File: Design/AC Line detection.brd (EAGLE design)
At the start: 17 x 20 mm, 14 parts

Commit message: version 1.0
* Added production files
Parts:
- moved FID2 19.4 mm to (4.49, 2.16)
- moved FID1 14.7 mm to (6.80, 19.0)
- moved LOGO1 1.22 mm to (9.08, 7.91)
- moved U$1 0.64 mm to (13.5, 1.25)
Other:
- board text added: "AC-IN"
- board text added: "~"
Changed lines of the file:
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@@
 <layer number="20" name="Dimension" color="15" fill="1" visible="yes" active="yes"/>
 <layer number="21" name="tPlace" color="7" fill="1" visible="yes" active="yes"/>
-<layer number="22" name="bPlace" color="7" fill="1" visible="yes" active="yes"/>
+<layer number="22" name="bPlace" color="7" fill="1" visible="no" active="yes"/>
 <layer number="23" name="tOrigins" color="15" fill="1" visible="yes" active="yes"/>
 <layer number="24" name="bOrigins" color="15" fill="1" visible="yes" active="yes"/>
@@
 <layer number="35" name="tGlue" color="7" fill="4" visible="no" active="yes"/>
 <layer number="36" name="bGlue" color="7" fill="5" visible="no" active="yes"/>
-<layer number="37" name="tTest" color="7" fill="1" visible="yes" active="yes"/>
-<layer number="38" name="bTest" color="7" fill="1" visible="yes" active="yes"/>
+<layer number="37" name="tTest" color="14" fill="1" visible="yes" active="yes"/>
+<layer number="38" name="bTest" color="11" fill="1" visible="yes" active="yes"/>
 <layer number="39" name="tKeepout" color="4" fill="11" visible="no" active="yes"/>
 <layer number="40" name="bKeepout" color="1" fill="11" visible="no" active="yes"/>
@@
 <layer number="118" name="Rect_Pads" color="7" fill="1" visible="no" active="no"/>
 <layer number="119" name="Logo" color="10" fill="1" visible="no" active="yes"/>
-<layer number="121" name="_tsilk" color="7" fill="1" visible="yes" active="yes"/>
-<layer number="122" name="_bsilk" color="7" fill="1" visible="yes" active="yes"/>
+<layer number="121" name="_tsilk" color="14" fill="1" visible="yes" active="yes"/>
+<layer number="122" name="_bsilk" color="11" fill="1" visible="yes" active="yes"/>
 <layer number="123" name="tTestmark" color="7" fill="1" visible="no" active="yes"/>
 <layer number="124" name="bTestmark" color="7" fill="1" visible="no" active="yes"/>
@@
 <wire x1="15" y1="20" x2="2" y2="20" width="0.2" layer="20"/>
 <wire x1="2" y1="20" x2="0" y2="18" width="0.2" layer="20" curve="90"/>
-<text x="11.32035" y="19.71355" size="1.27" layer="20" font="vector" ratio="10" rot="R180">S</text>
-<text x="13.91445" y="19.71355" size="1.27" layer="20" font="vector" ratio="10" rot="R180">+</text>
-<text x="16.39225" y="19.71355" size="1.27" layer="20" font="vector" ratio="10" rot="R180">-</text>
-<text x="2.6342" y="0.18125" size="0.8128" layer="121" font="vector">AC LINE DETECTOR</text>
+<text x="11.32035" y="19.71355" size="1.27" layer="121" font="vector" ratio="15" rot="R180">S</text>
+<text x="13.8428" y="19.71355" size="1.27" layer="121" font="vector" ratio="15" rot="R180">+</text>
+<text x="16.1063" y="19.726" size="1.27" layer="121" font="vector" ratio="15" rot="R180">-</text>
+<text x="2.67895" y="0.19615" size="0.8128" layer="121" font="vector" ratio="10">AC LINE DETECTOR</text>
 <dimension x1="15" y1="20" x2="15" y2="0" x3="24" y3="10" textsize="0.8128" layer="47"/>
 <dimension x1="0" y1="2" x2="17" y2="2" x3="8.5" y3="-6" textsize="0.8128" layer="47"/>
@@
 </polygon>
 <text x="9.77905" y="0.1472" size="1.016" layer="16" font="vector" ratio="15" rot="MR0">V1.0</text>
+<text x="7.93115" y="18.0174" size="1.4224" layer="122" ratio="15" rot="MR0">AC-IN</text>
+<text x="2.73015" y="12.7392" size="1.778" layer="122" font="vector" ratio="15">~</text>
+<text x="6.22115" y="12.72425" size="1.778" layer="122" font="vector" ratio="15">~</text>
 </plain>
 <attributes>
@@
 <elements>
 <element name="B1" library="rectifier" library_urn="urn:adsk.eagle:library:336" package="DBS" value="DBS107G" x="4.39805" y="6.71345"/>
-<element name="FID1" library="edwinRobotics" package="FIDUCIAL_1MM" value="FIDUCIAL&quot;&quot;" x="1.19485" y="5.33225"/>
-<element name="FID2" library="edwinRobotics" package="FIDUCIAL_1MM" value="FIDUCIAL&quot;&quot;" x="14.5243" y="18.77995"/>
-<element name="LOGO1" library="edwinRobotics" package="OSHW-LOGO-MINI" value="OSHW-LOGOMINI" x="7.86095" y="7.95625" rot="MR0"/>
-<element name="U$1" library="edwinRobotics" package="LOGO-9.5MMX4.5MM" value="LOGO-9.5MMX4.5MM" x="12.88175" y="1.2996" rot="MR0"/>
+<element name="FID1" library="edwinRobotics" package="FIDUCIAL_1MM" value="FIDUCIAL&quot;&quot;" x="6.802" y="18.9554"/>
+<element name="FID2" library="edwinRobotics" package="FIDUCIAL_1MM" value="FIDUCIAL&quot;&quot;" x="4.49175" y="2.1645"/>
+<element name="LOGO1" library="edwinRobotics" package="OSHW-LOGO-MINI" value="OSHW-LOGOMINI" x="9.08385" y="7.91165" rot="MR0"/>
+<element name="U$1" library="edwinRobotics" package="LOGO-9.5MMX4.5MM" value="LOGO-9.5MMX4.5MM" x="13.5252" y="1.255" rot="MR0"/>
 <element name="R1" library="edwinRobotics" package="R0603" value="10k" x="11.51635" y="13.9717"/>
 <element name="R2" library="edwinRobotics" package="R0603" value="390k" x="9.80565" y="2.4757" rot="R270"/>

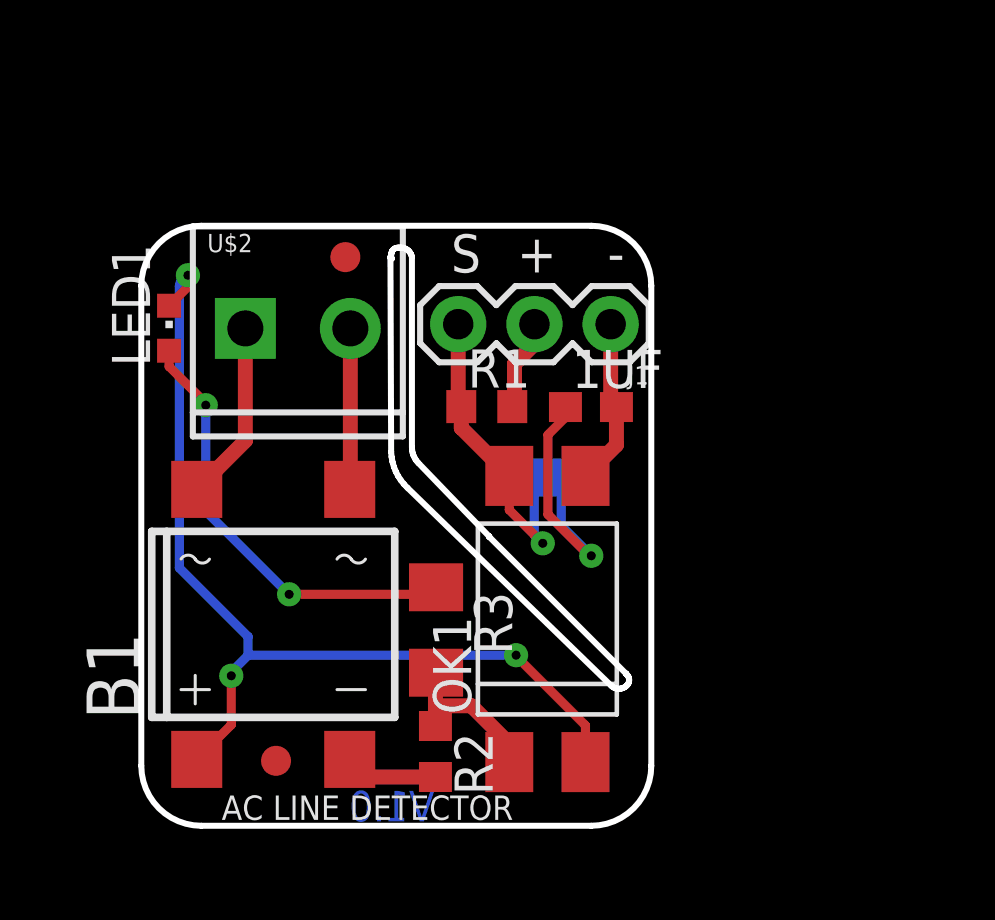
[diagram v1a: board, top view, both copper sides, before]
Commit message: Version 1.0
* updated schematics: Added electrolytic capacitor on board
* Updated board: increased dimesnions and new routing
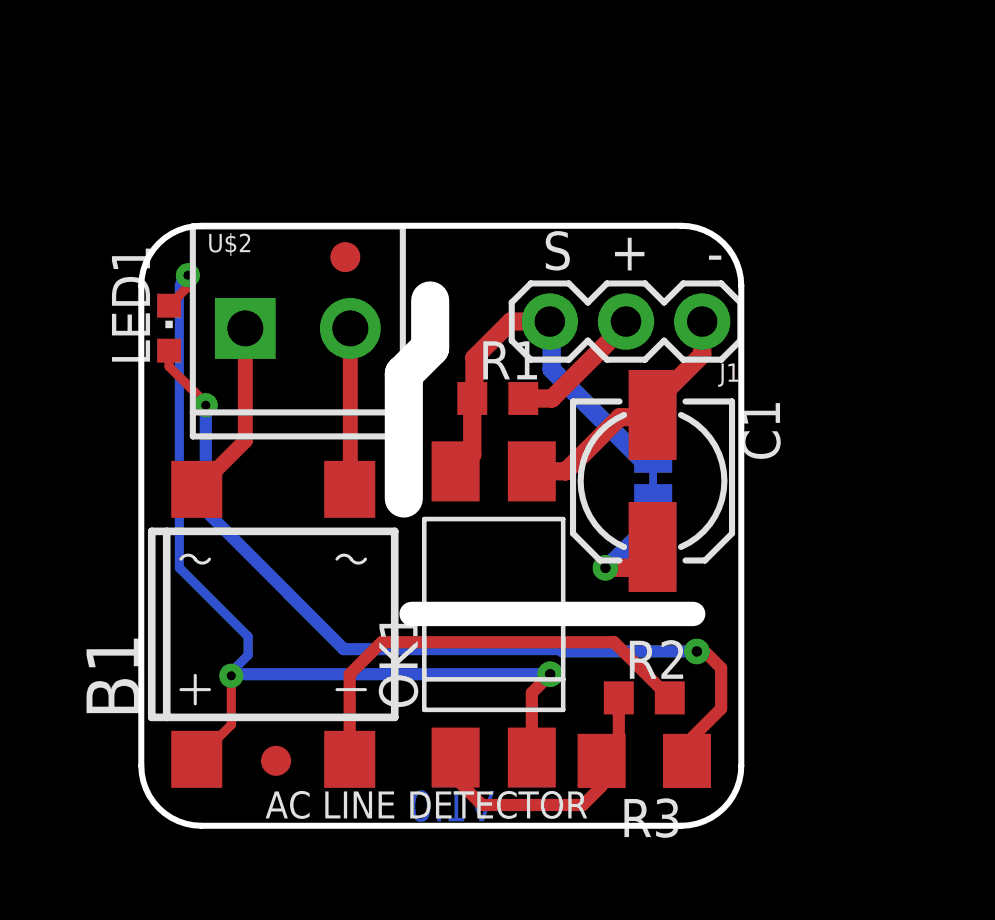
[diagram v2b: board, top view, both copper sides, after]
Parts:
- removed 1UF: (no value), edwinRobotics:C0603
- removed JP2: JUMPER-SMT_2_NO_SILK, edwinRobotics:SMT-JUMPER_2_NO_SILK
- added C1: (no value), edwinRobotics:153CLV-0505
- added JP1: JUMPER-SMT_2_NC_TRACE_NO-SILK, edwinRobotics:SMT-JUMPER_2_NC_TRACE_NO-SILK
- moved R3 8.20 mm to (16.8, 2.16), turned to 180 degrees
- moved R2 7.19 mm to (16.8, 4.26), turned to 0 degrees
- moved J1 3.05 mm to (18.7, 16.8)
- moved OK1 1.79 mm to (11.7, 7.04)
- moved LOGO1 1.15 mm to (9.89, 8.73)
- moved U$1 1.00 mm to (14.5, 1.25)
- moved R1 0.46 mm to (11.9, 14.2)
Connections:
- net GND: now also C1.-; no longer 1UF.2
- net N$2: now also C1.+, JP1.2; no longer 1UF.1, JP2.2
- net SIGNAL: now also JP1.1; no longer JP2.1
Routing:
- net N$3: track 14.8 -> 28.8 mm
- net N$1: track 3.10 -> 14.7 mm
- net +: track 5.38 -> 9.43 mm
- net N$2: track 8.94 -> 5.04 mm
- net GND: track 5.69 -> 8.72 mm
- net SIGNAL: track 10.8 -> 13.4 mm, vias 1 -> 0
- net 5V: track 3.05 -> 4.54 mm
- net -: track 32.8 -> 33.5 mm
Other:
- board size 17 x 20 mm -> 20 x 20 mm

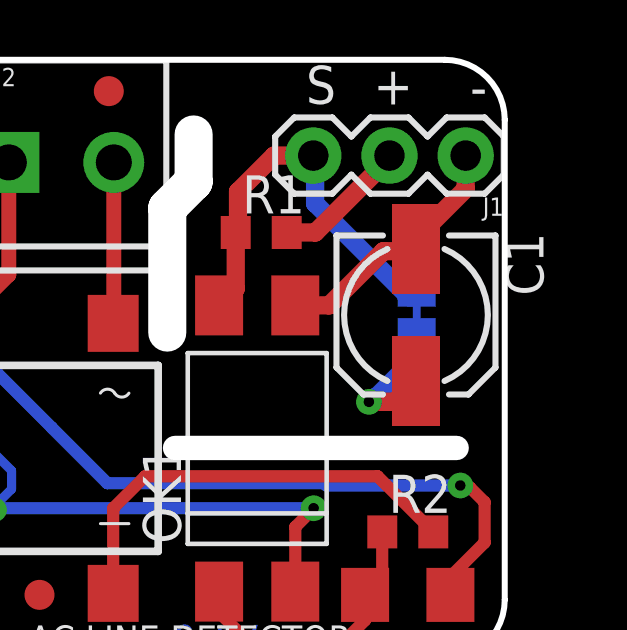
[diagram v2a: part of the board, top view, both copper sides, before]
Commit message: version 1.0 update:
* Updated Capacitor Pad Size
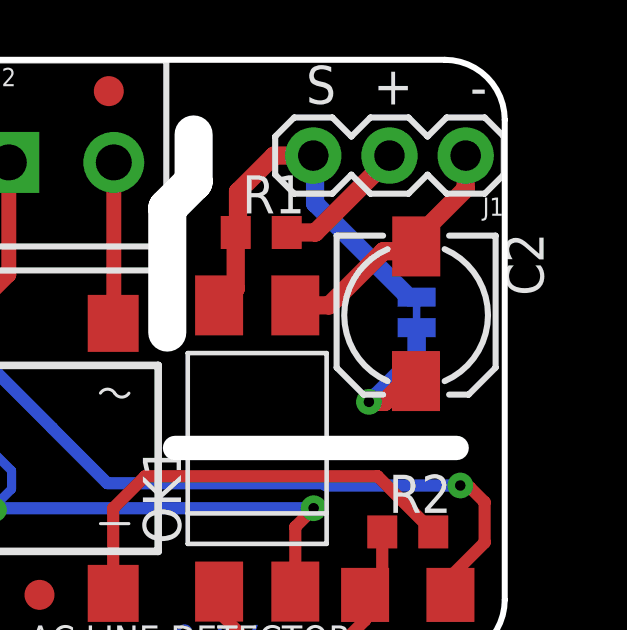
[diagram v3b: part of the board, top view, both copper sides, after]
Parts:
- removed C1: (no value), edwinRobotics:153CLV-0505
- added C2: 2.2uF, edwinRobotics:CAPACITOR-2.2UF_4X5MM_JENNY
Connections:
- net GND: now also C2.-; no longer C1.-
- net N$2: now also C2.+; no longer C1.+
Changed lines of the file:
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@@
 <layer number="19" name="Unrouted" color="6" fill="1" visible="yes" active="yes"/>
 <layer number="20" name="Dimension" color="15" fill="1" visible="yes" active="yes"/>
-<layer number="21" name="tPlace" color="7" fill="1" visible="yes" active="yes"/>
+<layer number="21" name="tPlace" color="7" fill="1" visible="no" active="yes"/>
 <layer number="22" name="bPlace" color="7" fill="1" visible="no" active="yes"/>
 <layer number="23" name="tOrigins" color="15" fill="1" visible="yes" active="yes"/>
@@
 <layer number="46" name="Milling" color="3" fill="1" visible="yes" active="yes"/>
 <layer number="47" name="Measures" color="7" fill="1" visible="yes" active="yes"/>
-<layer number="48" name="Document" color="7" fill="1" visible="yes" active="yes"/>
-<layer number="49" name="Reference" color="7" fill="1" visible="no" active="yes"/>
+<layer number="48" name="Document" color="7" fill="1" visible="no" active="yes"/>
+<layer number="49" name="Reference" color="7" fill="1" visible="yes" active="yes"/>
 <layer number="50" name="dxf" color="7" fill="1" visible="no" active="no"/>
 <layer number="51" name="tDocu" color="7" fill="1" visible="no" active="yes"/>
@@
 <layer number="101" name="Patch_Top" color="12" fill="4" visible="no" active="yes"/>
 <layer number="102" name="Vscore" color="7" fill="1" visible="no" active="yes"/>
-<layer number="103" name="fp3" color="7" fill="1" visible="yes" active="yes"/>
+<layer number="103" name="fp3" color="7" fill="1" visible="no" active="yes"/>
 <layer number="104" name="Name" color="7" fill="1" visible="no" active="yes"/>
 <layer number="105" name="Beschreib" color="9" fill="1" visible="no" active="yes"/>
@@
 <layer number="250" name="Descript" color="7" fill="1" visible="no" active="no"/>
 <layer number="251" name="SMDround" color="7" fill="1" visible="no" active="no"/>
-<layer number="253" name="Legend" color="10" fill="1" visible="no" active="yes"/>
+<layer number="253" name="Legend" color="10" fill="1" visible="yes" active="yes"/>
 <layer number="254" name="cooling" color="7" fill="1" visible="no" active="yes"/>
 <layer number="255" name="routoute" color="7" fill="1" visible="no" active="yes"/>
@@
 <element name="LED1" library="edwinRobotics" package="CHIPLED_0603" value="" x="0.92685" y="16.58635"/>
 <element name="JP1" library="edwinRobotics" package="SMT-JUMPER_2_NC_TRACE_NO-SILK" value="JUMPER-SMT_2_NC_TRACE_NO-SILK" x="17.06295" y="11.57915" rot="MR270"/>
-<element name="C1" library="edwinRobotics" package="153CLV-0505" value="" x="17.0413" y="11.493" rot="R270"/>
+<element name="C2" library="edwinRobotics" package="CAPACITOR-2.2UF_4X5MM_JENNY" value="2.2uF" x="17.0459" y="11.48835" rot="R270"/>
 </elements>
 <signals>
@@
 <contactref element="J1" pad="1"/>
 <contactref element="OK1" pad="3"/>
-<contactref element="C1" pad="-"/>
 <wire x1="18.6977" y1="16.80705" x2="18.6977" y2="15.6977" width="0.6096" layer="1"/>
 <wire x1="17" y1="14" x2="18.6977" y2="15.6977" width="0.6096" layer="1"/>
-<wire x1="17" y1="14" x2="17" y2="13.7343" width="0.6096" layer="1"/>
-<wire x1="17" y1="13.7343" x2="17.0413" y2="13.693" width="0.6096" layer="1"/>
+<wire x1="17" y1="13.7343" x2="17" y2="14" width="0.6096" layer="1"/>
 <wire x1="13.0183" y1="11.8135" x2="14.1482" y2="11.8135" width="0.6096" layer="1"/>
 <wire x1="14.1482" y1="11.8135" x2="15.9544" y2="13.6197" width="0.6096" layer="1"/>
-<wire x1="15.9544" y1="13.6197" x2="16.6197" y2="13.6197" width="0.6096" layer="1"/>
+<wire x1="16.6197" y1="13.6197" x2="15.9544" y2="13.6197" width="0.6096" layer="1"/>
 <wire x1="16.6197" y1="13.6197" x2="17" y2="14" width="0.6096" layer="1"/>
+<contactref element="C2" pad="-"/>
+<wire x1="16.693" y1="13.693" x2="16.6197" y2="13.6197" width="0.6096" layer="1"/>
+<wire x1="17.0413" y1="13.76975" x2="17.0494" y2="13.77785" width="0.6096" layer="1"/>
+<wire x1="17.0494" y1="13.77785" x2="17.04355" y2="13.77785" width="0.6096" layer="1"/>
+<wire x1="17.04355" y1="13.77785" x2="17" y2="13.7343" width="0.6096" layer="1"/>
 </signal>
 <signal name="5V">
@@
 <signal name="N$2">
 <contactref element="JP1" pad="2"/>
-<contactref element="C1" pad="+"/>
 <wire x1="17.06295" y1="11.07115" x2="17.06295" y2="10.1043" width="0.6096" layer="16"/>
 <wire x1="17.06295" y1="10.1043" x2="15.69065" y2="8.732" width="0.6096" layer="16"/>
@@
 <wire x1="15.60555" y1="8.732" x2="15.47175" y2="8.5982" width="0.6096" layer="16"/>
 <via x="15.47175" y="8.5982" extent="1-16" drill="0.35"/>
-<wire x1="15.47175" y1="8.5982" x2="16.3465" y2="8.5982" width="0.6096" layer="1"/>
-<wire x1="16.3465" y1="8.5982" x2="17.0413" y2="9.293" width="0.6096" layer="1"/>
+<wire x1="16" y1="8.5982" x2="15.47175" y2="8.5982" width="0.6096" layer="1"/>
+<contactref element="C2" pad="+"/>
+<wire x1="16.6948" y1="9.293" x2="16" y2="8.5982" width="0.6096" layer="1"/>
+<wire x1="17.0413" y1="9.29145" x2="17.0414" y2="9.29135" width="0.6096" layer="1"/>
+<wire x1="17.0414" y1="9.29135" x2="16.69645" y2="9.29135" width="0.6096" layer="1"/>
+<wire x1="16.69645" y1="9.29135" x2="16.6948" y2="9.293" width="0.6096" layer="1"/>
 </signal>
 <signal name="N$3">

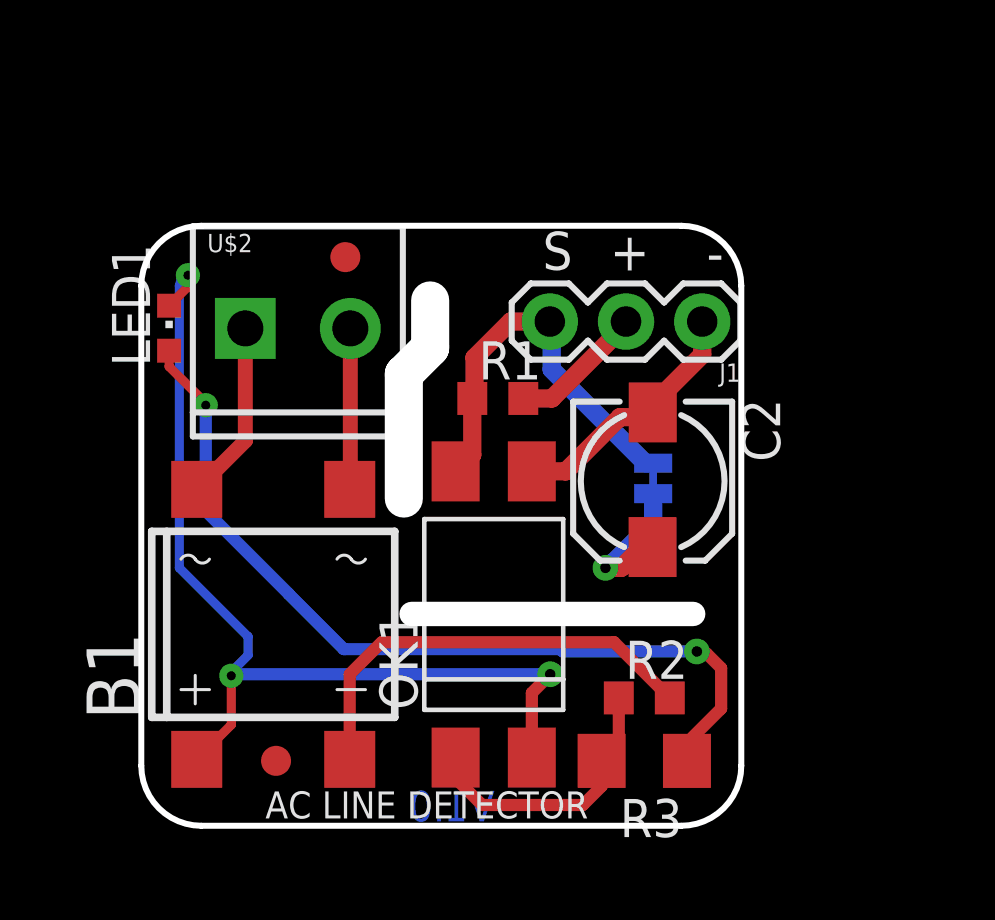
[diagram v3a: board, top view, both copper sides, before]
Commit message: Version 2.0:
Major Changes:
*Updated Design FIles
* Updated the board Size
* Added mounting Holes
* Added Debug LED and enable/Disbale Jumper
* Replaced Screw terminal with KF126
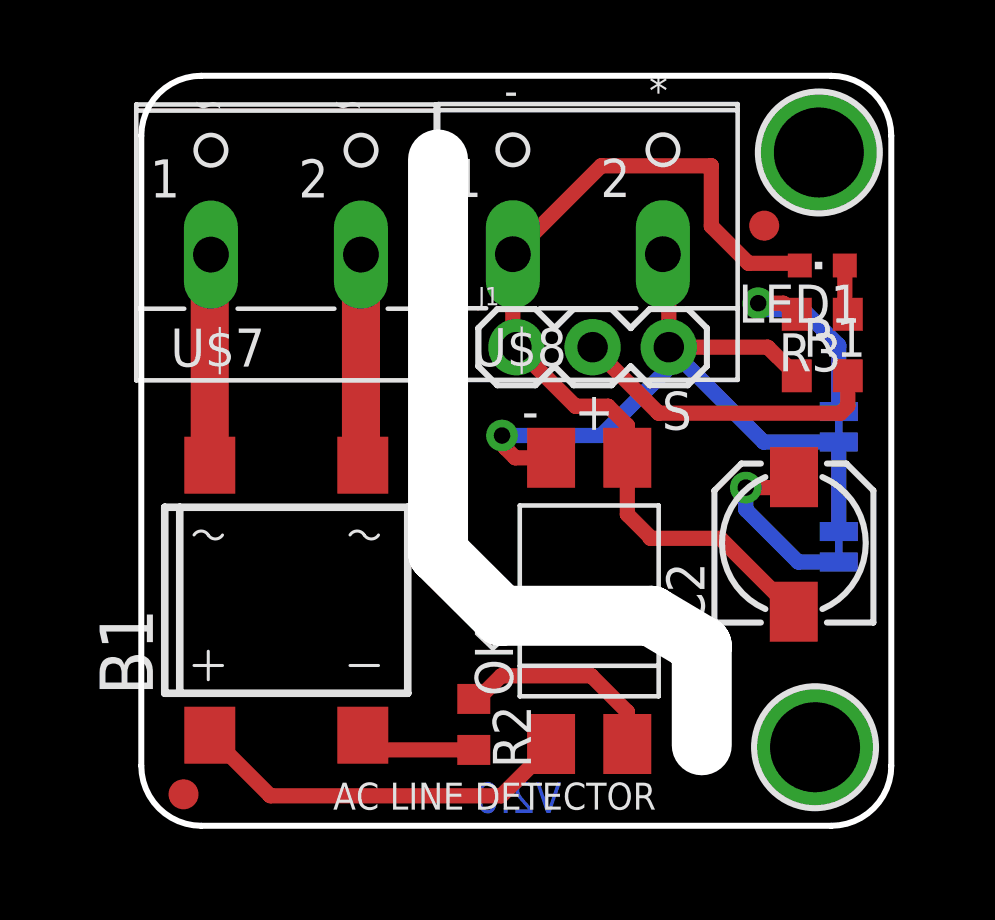
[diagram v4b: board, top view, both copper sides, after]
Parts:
- removed U$2: SCREW_TERMINALS-2P-3.5MM, edwinRobotics:SCREWTERMINAL-3.5MM-2
- added JP2: JUMPER-SMT_2_NC_TRACE_NO-SILK, edwinRobotics:SMT-JUMPER_2_NC_TRACE_NO-SILK
- added U$5, U$6: MOUNTINGHOLE3.0THIN, edwinRobotics:MOUNTINGHOLE_3.0_PLATEDTHIN
- added U$7, U$8: SCREW_TERMINALS-2P-5MM, edwinRobotics:W237-102
- R3: value 10k -> (none); device edwinRobotics:R1206 -> edwinRobotics:R0603
- moved LED1 21.9 mm to (22.7, 18.7), turned to 90 degrees
- moved R3 16.0 mm to (22.7, 17.1)
- moved FID1 14.0 mm to (20.8, 20.0)
- moved R1 10.8 mm to (22.7, 15.0)
- moved JP1 6.59 mm to (23.2, 9.30)
- moved J1 6.25 mm to (12.5, 16.0), turned to 0 degrees
- moved R2 5.75 mm to (11.1, 3.38), turned to 270 degrees
- moved C2 5.14 mm to (21.8, 9.42), turned to 90 degrees
- moved LOGO1 5.06 mm to (4.83, 8.74)
- moved FID2 3.28 mm to (1.41, 1.05)
- moved OK1 3.21 mm to (14.9, 7.50)
- moved U$1 2.87 mm to (17.2, 2.21)
- moved B1 0.91 mm to (4.83, 7.52)
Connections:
- new net N$4: JP2.1, R3.2
- net +: now also B1.+; no longer R2.1, R3.2
- net -: now also R2.1; no longer B1.+, LED1.C
- net AC_L: now also U$7.2; no longer U$2.2
- net AC_N: now also U$7.1; no longer U$2.1
- net GND: now also LED1.C, U$8.1
- net SIGNAL: now also JP2.2, U$8.2
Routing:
- net N$3: track 28.8 -> 1.89 mm, vias 2 -> 0
- net -: track 33.5 -> 7.01 mm, vias 3 -> 0
- net GND: track 8.85 -> 31.2 mm
- net SIGNAL: track 13.4 -> 27.1 mm, vias 0 -> 1
- net N$1: track 14.7 -> 3.90 mm
- net N$4: track 0.00 -> 7.03 mm, vias 0 -> 1
- net 5V: track 4.54 -> 10.5 mm
- net +: track 9.43 -> 13.0 mm
- net AC_L: track 5.37 -> 7.05 mm
- net N$2: track 5.04 -> 6.31 mm
- net AC_N: track 6.04 -> 7.04 mm
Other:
- board size 20 x 20 mm -> 25 x 25 mm
- board text added: "*"
- board text added: "Detection"
- board text added: "Status LED"
- board text added: "V2.0"
- board text added: "Zero Crossing"
- board text removed: "V1.0"
